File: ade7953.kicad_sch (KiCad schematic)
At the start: 58 parts, among them J6 H/L1, J7 N/L2, J8 VOLTS, U2 ADE7953xCP, Y1 3.58MHz

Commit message: update jumper numbers
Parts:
- renumbered JP8 to JP6, JP9 to JP7, JP10 to JP8, JP11 to JP9
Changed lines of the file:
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@@
 		(dnp no)
 		(fields_autoplaced yes)
-		(property "Reference" "JP8"
+		(property "Reference" "JP6"
 			(at 59.69 106.68 0)
 			(effects
@@
 			(project "wing-combo"
 				(path "/586efc0f-7de2-49a7-ac21-ecfef2f716d6/3f0e9b91-fe15-47d5-84d6-aa71b368b91e/03adfa84-7245-4a0a-b28d-db7d09a8f743"
-					(reference "JP8")
+					(reference "JP6")
 					(unit 1)
 				)
@@
 		(on_board yes)
 		(dnp no)
-		(property "Reference" "JP9"
+		(property "Reference" "JP7"
 			(at 59.69 144.78 0)
 			(effects
@@
 			(project "wing-combo"
 				(path "/586efc0f-7de2-49a7-ac21-ecfef2f716d6/3f0e9b91-fe15-47d5-84d6-aa71b368b91e/03adfa84-7245-4a0a-b28d-db7d09a8f743"
-					(reference "JP9")
+					(reference "JP7")
 					(unit 1)
 				)
@@
 		(dnp no)
 		(fields_autoplaced yes)
-		(property "Reference" "JP10"
+		(property "Reference" "JP8"
 			(at 59.69 153.67 0)
 			(effects
@@
 			(project "wing-combo"
 				(path "/586efc0f-7de2-49a7-ac21-ecfef2f716d6/3f0e9b91-fe15-47d5-84d6-aa71b368b91e/03adfa84-7245-4a0a-b28d-db7d09a8f743"
-					(reference "JP10")
+					(reference "JP8")
 					(unit 1)
 				)
@@
 		(on_board yes)
 		(dnp no)
-		(property "Reference" "JP11"
+		(property "Reference" "JP9"
 			(at 59.69 191.77 0)
 			(effects
@@
 			(project "wing-combo"
 				(path "/586efc0f-7de2-49a7-ac21-ecfef2f716d6/3f0e9b91-fe15-47d5-84d6-aa71b368b91e/03adfa84-7245-4a0a-b28d-db7d09a8f743"
-					(reference "JP11")
+					(reference "JP9")
 					(unit 1)
 				)

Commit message: update jumper numbers pt2
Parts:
- renumbered JP6 to JP10, JP7 to JP11
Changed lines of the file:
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@@
 		(on_board yes)
 		(dnp no)
-		(property "Reference" "JP7"
+		(property "Reference" "JP11"
 			(at 124.46 161.29 0)
 			(effects
@@
 			(project "wing-combo"
 				(path "/586efc0f-7de2-49a7-ac21-ecfef2f716d6/3f0e9b91-fe15-47d5-84d6-aa71b368b91e/03adfa84-7245-4a0a-b28d-db7d09a8f743"
-					(reference "JP7")
+					(reference "JP11")
 					(unit 1)
 				)
@@
 		(on_board yes)
 		(dnp no)
-		(property "Reference" "JP6"
+		(property "Reference" "JP10"
 			(at 123.19 181.61 0)
 			(effects
@@
 			(project "wing-combo"
 				(path "/586efc0f-7de2-49a7-ac21-ecfef2f716d6/3f0e9b91-fe15-47d5-84d6-aa71b368b91e/03adfa84-7245-4a0a-b28d-db7d09a8f743"
-					(reference "JP6")
-					(unit 1)
-				)
+					(reference "JP10")
+					(unit 1)
+				)

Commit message: update reference values for better ibom
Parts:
- renumbered IN-AUX-1 to J23, binary-current1 to J24, J6 to J5, J7 to J6, J8 to J7
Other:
- moved on the sheet: J24
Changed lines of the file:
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@@
 	(wire
 		(pts
-			(xy 102.87 97.79) (xy 105.41 97.79)
+			(xy 97.79 99.06) (xy 100.33 99.06)
 		)
 		(stroke
@@
 	(wire
 		(pts
-			(xy 102.87 95.25) (xy 106.68 95.25)
+			(xy 97.79 96.52) (xy 101.6 96.52)
 		)
 		(stroke
@@
 	(wire
 		(pts
-			(xy 102.87 92.71) (xy 105.41 92.71)
+			(xy 97.79 93.98) (xy 100.33 93.98)
 		)
 		(stroke
@@
 	(wire
 		(pts
-			(xy 105.41 97.79) (xy 105.41 99.06)
+			(xy 100.33 99.06) (xy 100.33 100.33)
 		)
 		(stroke
@@
 	(wire
 		(pts
-			(xy 105.41 92.71) (xy 105.41 91.44)
+			(xy 100.33 93.98) (xy 100.33 92.71)
 		)
 		(stroke
@@
 	)
 	(rectangle
-		(start 83.185 85.09)
+		(start 83.185 81.28)
 		(end 126.365 125.73)
 		(stroke
@@
 	(text "connect a \nbreakout board \nwith simple i/o"
 		(exclude_from_sim no)
-		(at 116.332 100.33 0)
+		(at 111.252 101.6 0)
 		(effects
 			(font
@@
 	(text "Backup Plan"
 		(exclude_from_sim no)
-		(at 94.488 88.646 0)
+		(at 94.488 84.836 0)
 		(effects
 			(font
@@
 	(global_label "binary-current"
 		(shape input)
-		(at 106.68 95.25 0)
+		(at 101.6 96.52 0)
 		(fields_autoplaced yes)
 		(effects
@@
 		)
 		(property "Intersheetrefs" "${INTERSHEET_REFS}"
-			(at 123.8165 95.25 0)
+			(at 118.7365 96.52 0)
 			(effects
 				(font
@@
 		(on_board yes)
 		(dnp no)
-		(property "Reference" "J7"
+		(property "Reference" "J6"
 			(at 68.58 64.77 0)
 			(effects
@@
 			(project "wing-combo"
 				(path "/586efc0f-7de2-49a7-ac21-ecfef2f716d6/3f0e9b91-fe15-47d5-84d6-aa71b368b91e/03adfa84-7245-4a0a-b28d-db7d09a8f743"
-					(reference "J7")
+					(reference "J6")
 					(unit 1)
 				)
@@
 		(dnp yes)
 		(fields_autoplaced yes)
-		(property "Reference" "IN-AUX-1"
+		(property "Reference" "J23"
 			(at 45.72 73.6599 0)
 			(effects
@@
 			(project "wing-combo"
 				(path "/586efc0f-7de2-49a7-ac21-ecfef2f716d6/3f0e9b91-fe15-47d5-84d6-aa71b368b91e/03adfa84-7245-4a0a-b28d-db7d09a8f743"
-					(reference "IN-AUX-1")
+					(reference "J23")
 					(unit 1)
 				)
@@
 		(on_board yes)
 		(dnp no)
-		(property "Reference" "J8"
+		(property "Reference" "J7"
 			(at 113.03 64.77 0)
 			(effects
@@
 			(project "wing-combo"
 				(path "/586efc0f-7de2-49a7-ac21-ecfef2f716d6/3f0e9b91-fe15-47d5-84d6-aa71b368b91e/03adfa84-7245-4a0a-b28d-db7d09a8f743"
-					(reference "J8")
+					(reference "J7")
 					(unit 1)
 				)
@@
 	(symbol
 		(lib_id "power:GND")
-		(at 105.41 99.06 0)
+		(at 100.33 100.33 0)
 		(unit 1)
 		(exclude_from_sim no)
@@
 		(dnp no)
 		(property "Reference" "#PWR022"
-			(at 105.41 105.41 0)
+			(at 100.33 106.68 0)
 			(effects
 				(font
@@
 		)
 		(property "Value" "GND"
-			(at 105.41 102.87 0)
+			(at 100.33 104.14 0)
 			(effects
 				(font
@@
 		)
 		(property "Footprint" ""
-			(at 105.41 99.06 0)
+			(at 100.33 100.33 0)
 			(effects
 				(font
@@
 		)
 		(property "Datasheet" ""
-			(at 105.41 99.06 0)
+			(at 100.33 100.33 0)
 			(effects
 				(font
@@
 		)
 		(property "Description" "Power symbol creates a global label with name \"GND\" , ground"
-			(at 105.41 99.06 0)
+			(at 100.33 100.33 0)
 			(effects
 				(font
@@
 	(symbol
 		(lib_id "Connector:Conn_01x03_Socket")
-		(at 97.79 95.25 0)
+		(at 92.71 96.52 0)
 		(mirror y)
 		(unit 1)
@@
 		(on_board yes)
 		(dnp no)
-		(property "Reference" "binary-current1"
-			(at 102.616 100.33 0)
+		(property "Reference" "J24"
+			(at 97.536 101.6 0)
 			(effects
 				(font
@@
 		)
 		(property "Value" "Conn_01x03_Female"
-			(at 95.25 93.98 0)
+			(at 90.17 95.25 0)
 			(effects
 				(font
@@
 		)
 		(property "Footprint" "Connector_JST:JST_PH_B3B-PH-K_1x03_P2.00mm_Vertical"
-			(at 97.79 95.25 0)
+			(at 92.71 96.52 0)
 			(effects
 				(font
@@
 		)
 		(property "Datasheet" "~"
-			(at 97.79 95.25 0)
+			(at 92.71 96.52 0)
 			(effects
 				(font
@@
 		)
 		(property "Description" "Generic connector, single row, 01x03, script generated"
-			(at 97.79 95.25 0)
+			(at 92.71 96.52 0)
 			(effects
 				(font
@@
 		)
 		(property "JLCPCB Part #" "C131339"
-			(at 97.79 95.25 0)
+			(at 92.71 96.52 0)
 			(effects
 				(font
@@
 			(project "wing-combo"
 				(path "/586efc0f-7de2-49a7-ac21-ecfef2f716d6/3f0e9b91-fe15-47d5-84d6-aa71b368b91e/03adfa84-7245-4a0a-b28d-db7d09a8f743"
-					(reference "binary-current1")
+					(reference "J24")
 					(unit 1)
 				)
@@
 		(on_board yes)
 		(dnp no)
-		(property "Reference" "J6"
+		(property "Reference" "J5"
 			(at 24.13 64.77 0)
 			(effects
@@
 			(project "wing-combo"
 				(path "/586efc0f-7de2-49a7-ac21-ecfef2f716d6/3f0e9b91-fe15-47d5-84d6-aa71b368b91e/03adfa84-7245-4a0a-b28d-db7d09a8f743"
-					(reference "J6")
+					(reference "J5")
 					(unit 1)
 				)
@@
 	(symbol
 		(lib_id "power:+3.3V")
-		(at 105.41 91.44 0)
+		(at 100.33 92.71 0)
 		(mirror y)
 		(unit 1)
@@
 		(dnp no)
 		(property "Reference" "#PWR024"
-			(at 105.41 95.25 0)
+			(at 100.33 96.52 0)
 			(effects
 				(font
@@
 		)
 		(property "Value" "+3.3V"
-			(at 110.49 90.17 0)
+			(at 105.41 91.44 0)
 			(effects
 				(font
@@
 		)
 		(property "Footprint" ""
-			(at 105.41 91.44 0)
+			(at 100.33 92.71 0)
 			(effects
 				(font
@@
 		)
 		(property "Datasheet" ""
-			(at 105.41 91.44 0)
+			(at 100.33 92.71 0)
 			(effects
 				(font
@@
 		)
 		(property "Description" "Power symbol creates a global label with name \"+3.3V\""
-			(at 105.41 91.44 0)
+			(at 100.33 92.71 0)
 			(effects
 				(font

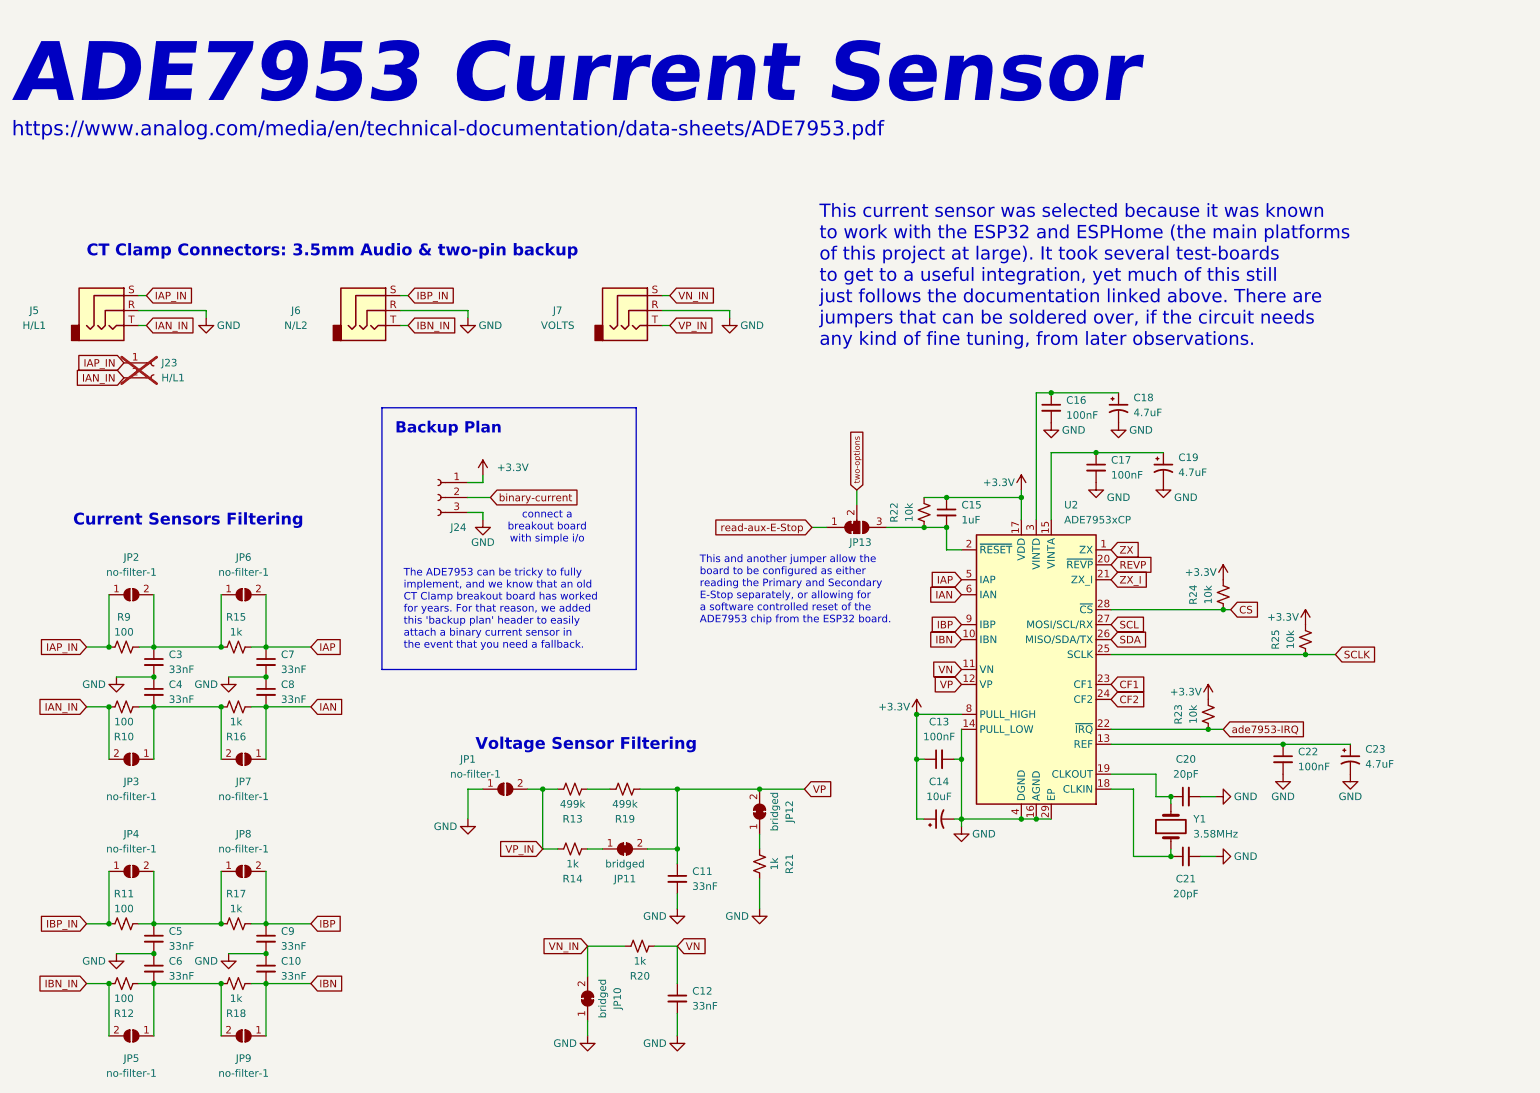
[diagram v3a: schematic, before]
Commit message: 5v binary current and cleanup
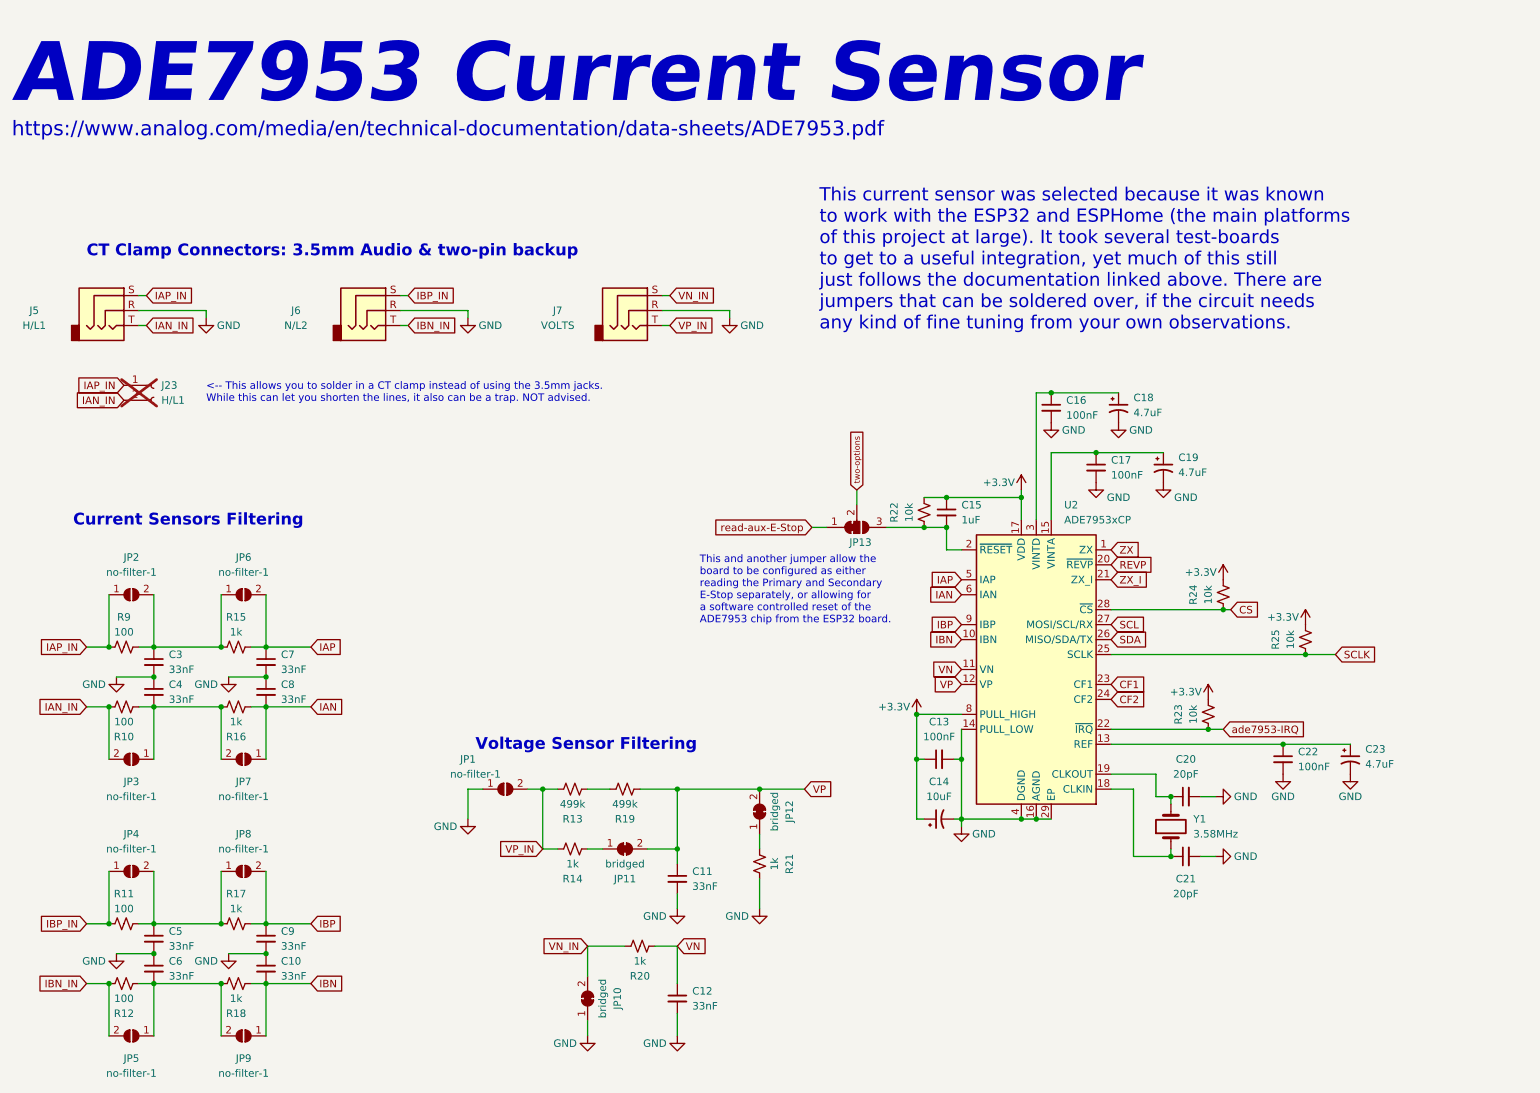
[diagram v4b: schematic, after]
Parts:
- removed J24: Conn_01x03_Female, Connector_JST:JST_PH_B3B-PH-K_1x03_P2.00mm_Vertical, symbol Connector:Conn_01x03_Socket
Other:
- note added: "<-- This allows you to solder in a CT clamp instead of using the 3.5mm jacks. While this can let you shorten the lines, it also can be a trap. NOT advised."
- note added: "This current sensor was selected because it was known to work with the ESP32 and ESPHome (the main platforms of this project at large). It took several test-boards to get to a useful integration, yet much of this still just follows the documentation linked above. There are jumpers that can be soldered over, if the circuit needs any kind of fine tuning from your own observations."
- note removed: "Backup Plan"
- note removed: "The ADE7953 can be tricky to fully implement, and we know that an old CT Clamp breakout board has worked for years. For that reason, we added this 'backup plan' header to easily attach a binary current sensor in the event that you need a fallback."
- note removed: "This current sensor was selected because it was known to work with the ESP32 and ESPHome (the main platforms of this project at large). It took several test-boards to get to a useful integration, yet much of this still just follows the documentation linked above. There are jumpers that can be soldered over, if the circuit needs any kind of fine tuning, from later observations."
- note removed: "connect a breakout board with simple i/o"
- moved on the sheet: J23

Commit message: close enough for 3D export
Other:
- note added: "(like this)"
- note added: "- a WCS1800 on board, configured for AC"
- note added: "- on-board shunt resistor options"
- note added: "- the TI ADS1115 over I2C"
- note added: "If the ADE7953 (this page) is not working for you, try new I2C resistors. Or fully bail on the ADE7953 and use an "AC current sensing relay" on our 'backup plan' bin-cur connector. [sometimes we do, no shame] - Previous page in schematic - We really like the M3050 for this job"
- note added: "In the future, we may get a more elegant solution to monitor the electric current drawn by the tool. There are several possible future options to explore:"
- note added: "Measuring AC Current is hard."
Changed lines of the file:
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@@
+		)
+	)
+	(rectangle
+		(start 81.788 87.122)
+		(end 131.318 130.302)
+		(stroke
+			(width 0)
+			(type default)
+		)
+		(fill
+			(type none)
+		)
+	)
+	(text "If the ADE7953 (this page) is not working for \nyou, try new I2C resistors. Or fully bail on \nthe ADE7953 and use an \"AC current sensing \nrelay\" on our 'backup plan' bin-cur \nconnector. [sometimes we do, no shame]\n  - Previous page in schematic\n  - We really like the M3050 for this job"
+		(exclude_from_sim no)
+		(at 83.312 100.584 0)
+		(effects
+			(font
+				(size 1.27 1.27)
+			)
+			(justify left)
 		)
 	)
@@
 			)
 			(justify left bottom)
+		)
+	)
+	(text "- a WCS1800 on board, configured for AC"
+		(exclude_from_sim no)
+		(at 85.852 126.492 0)
+		(effects
+			(font
+				(size 1.27 1.27)
+			)
+			(justify left)
+		)
+	)
+	(text "- the TI ADS1115 over I2C"
+		(exclude_from_sim no)
+		(at 85.852 120.396 0)
+		(effects
+			(font
+				(size 1.27 1.27)
+			)
+			(justify left)
+			(href "https://www.ti.com/product/ADS1115")
+		)
+	)
+	(text "- on-board shunt resistor options"
+		(exclude_from_sim no)
+		(at 85.852 123.444 0)
+		(effects
+			(font
+				(size 1.27 1.27)
+			)
+			(justify left)
+		)
+	)
+	(text "Measuring AC Current is hard."
+		(exclude_from_sim no)
+		(at 106.68 90.17 0)
+		(effects
+			(font
+				(size 1.905 1.905)
+				(thickness 0.381)
+				(bold yes)
+			)
+		)
+	)
+	(text "(like this)"
+		(exclude_from_sim no)
+		(at 117.856 120.396 0)
+		(effects
+			(font
+				(size 1.27 1.27)
+			)
+			(href "https://a.co/d/iXRwzz9")
 		)
 	)
@@
 		)
 	)
+	(text "In the future, we may get a more elegant \nsolution to monitor the electric current \ndrawn by the tool. There are several possible\nfuture options to explore: "
+		(exclude_from_sim no)
+		(at 83.566 114.554 0)
+		(effects
+			(font
+				(size 1.27 1.27)
+			)
+			(justify left)
+		)
+	)
